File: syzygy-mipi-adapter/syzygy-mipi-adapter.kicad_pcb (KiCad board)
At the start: 4 copper layers, 45 x 70 mm, 79 parts, among them J1 Conn_02x06_Odd_Even, J10 501951-2230, J2 SYZYGY_STD, J3 Conn_01x02, J5 SM03B-SRSS-TB, J8 501951-2230, J9 501951-2230, Q1 DMG1024UV-7, Q2 DMG1024UV-7, U1 RP2350_80QFN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

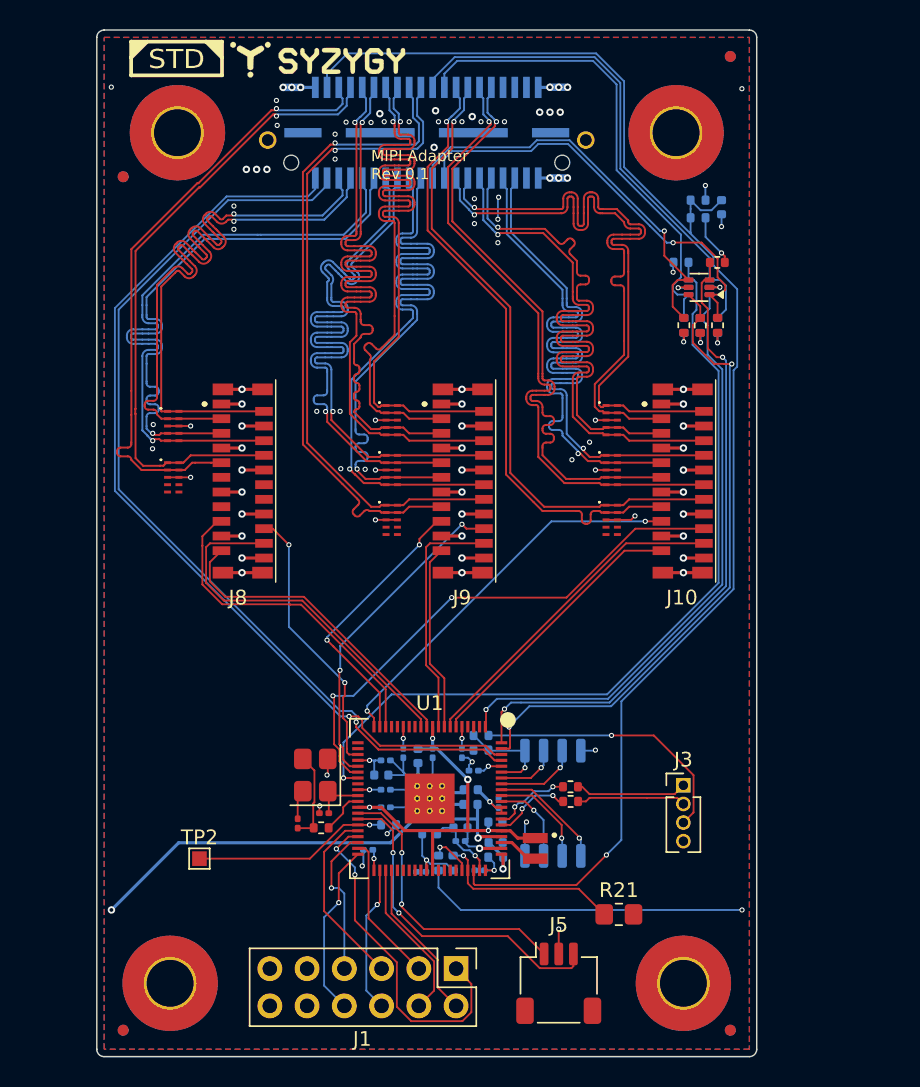
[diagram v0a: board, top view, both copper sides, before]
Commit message: Add USB connector and 3.3V regulator to Syzygy MIPI adapter
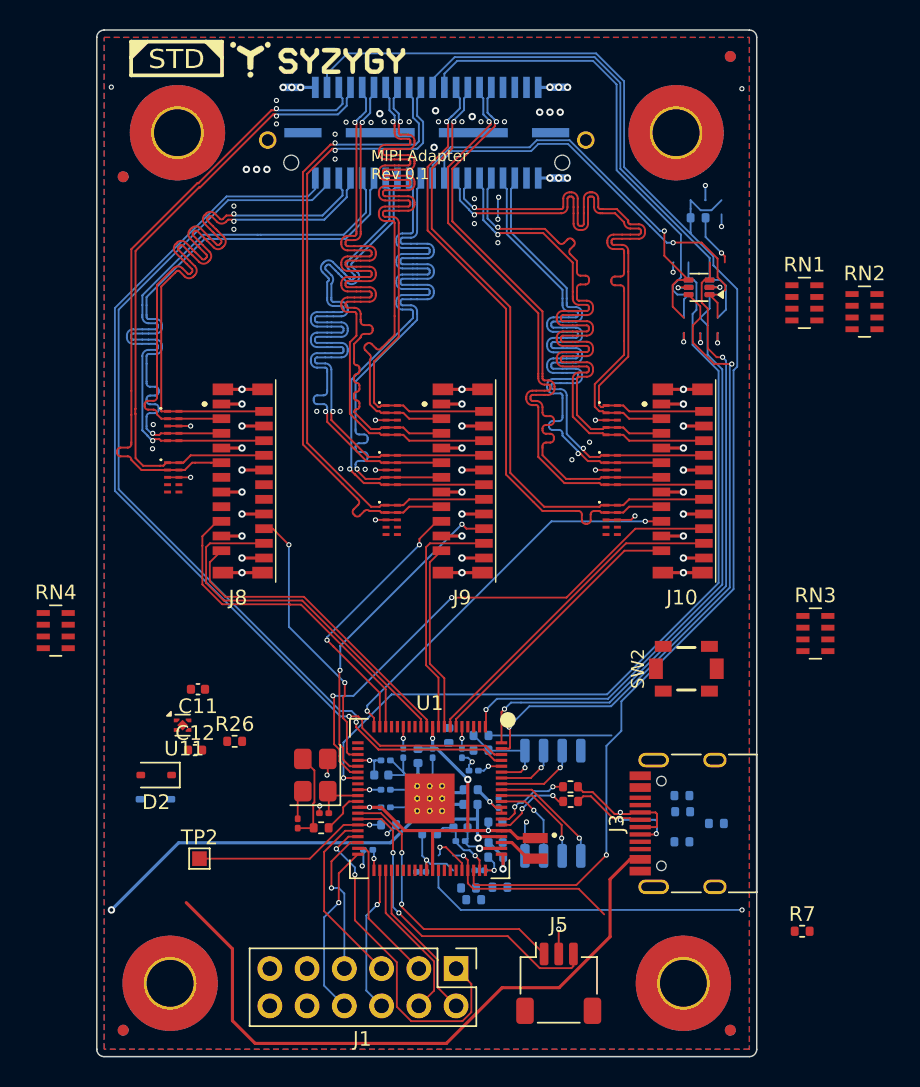
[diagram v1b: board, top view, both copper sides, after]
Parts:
- removed C44: 0.1uF, Capacitor_SMD:C_0402_1005Metric
- removed R13, R14, R15, R16, R17: 4.7K, Resistor_SMD:R_0402_1005Metric
- removed R19: ~, Resistor_SMD:R_0402_1005Metric
- removed R20: 10K, Resistor_SMD:R_0402_1005Metric
- removed R21: 0805, Resistor_SMD:R_0805_2012Metric_Pad1.20x1.40mm_HandSolder
- added C11: 10u, Capacitor_SMD:C_0402_1005Metric, F.Cu at (106.9, 105.0)
- added C12: 10u, Capacitor_SMD:C_0402_1005Metric, F.Cu at (106.7, 109.1)
- added D1: 1N5819WS, Diode_SMD:D_SOD-323, B.Cu at (104.0, 112.5)
- added D2: 1N5819WS, Diode_SMD:D_SOD-323, F.Cu at (104.0, 110.8)
- added LOGO3: OSHW logo, CUSTOM:OSHW_Dual_0.1_Scale_2140, F.Cu at (159.2, 97.0)
- added LOGO4: tinyAI logo, CUSTOM:tinyAI_logo, F.Cu at (159.9, 93.8)
- added R22: 5.1K, Resistor_SMD:R_0402_1005Metric, B.Cu at (139.9, 115.3)
- added R23: 56K, Resistor_SMD:R_0402_1005Metric, B.Cu at (139.9, 112.2)
- added R24: 56K, Resistor_SMD:R_0402_1005Metric, B.Cu at (142.2, 114.1)
- added R25: 5.1K, Resistor_SMD:R_0402_1005Metric, B.Cu at (139.9, 113.3)
- added R26: 10K, Resistor_SMD:R_0402_1005Metric, F.Cu at (109.4, 108.5)
- added R27: 15K, Resistor_SMD:R_0402_1005Metric, B.Cu at (124.0, 108.1)
- added RN1: 4.7K, Resistor_SMD:R_Array_Concave_4x0603, F.Cu at (148.2, 78.6)
- added RN2: 4.7K, Resistor_SMD:R_Array_Concave_4x0603, F.Cu at (152.3, 79.2)
- added RN3: 4.7K, Resistor_SMD:R_Array_Concave_4x0603, F.Cu at (149.0, 101.2)
- added RN4: 4.7K, Resistor_SMD:R_Array_Concave_4x0603, F.Cu at (97.2, 101.0)
- added SW2: CS1213AGF260, CUSTOM:PTS820J25KSMTRLFS, F.Cu at (140.2, 103.5)
- added U11: NCP115AMX330TCG, Package_DFN_QFN:OnSemi_XDFN4-1EP_1.0x1.0mm_EP0.52x0.52mm, F.Cu at (105.8, 107.4)
- J3: value Conn_01x02 -> USB_C_Receptacle_USB2.0_16P; footprint Connector_PinHeader_1.27mm:PinHeader_1x04_P1.27mm_Vertical -> Connector_USB:USB_C_Receptacle_HRO_TYPE-C-31-M-12
- R10: value 4.7K -> 10K; moved to B.Cu
- R11: value 4.7K -> 56K; moved to B.Cu
- R12: value 4.7K -> 56K
- R7: value 100 -> 10K; moved to F.Cu
- moved R10 45.1 mm to (127.5, 118.5)
- moved R12 45.1 mm to (125.3, 118.5)
- moved R11 42.1 mm to (125.7, 119.3), turned to 0 degrees
- moved R7 25.2 mm to (148.1, 121.5), turned to 0 degrees
- moved J3 2.82 mm to (141.1, 114.1), turned to 90 degrees
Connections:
- C1 pad 1: P5VD -> Net-(D1-K)
- J2 pad 40: P3V3D -> /SZG_3V3
- R10 pad 1: P3V3D -> /SZG_3V3
- R10 pad 2: /SCL_HOST_3V3 -> Net-(U1-GPIO44_ADC4)
- R11 pad 1: P3V3D -> Net-(U1-GPIO44_ADC4)
- R11 pad 2: /SDA_HOST_3V3 -> GND
- R12 pad 1: P3V3D -> Net-(U1-GPIO45_ADC5)
- R12 pad 2: /GPIO_HOST_3V3 -> GND
- R18 pad 1: P3V3D -> /R_GA
- R18 pad 2: /R_GA -> /SZG_3V3
- R5 pad 1: Net-(J3-Pin_1) -> /USB_D+
- R6 pad 1: Net-(J3-Pin_2) -> /USB_D-
- R8 pad 1: /USB_BOOTn -> Net-(R8-Pad1)
- U1 pad 55: unconnected-(U1-GPIO44_ADC4-Pad55) -> Net-(U1-GPIO44_ADC4)
- U1 pad 64: P5VD -> Net-(D1-K)
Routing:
- net PVBUS: track 0.00 -> 45.3 mm
- net P5VD: track 46.7 -> 15.1 mm, vias 6 -> 4
- net Net-(D1-K): track 0.00 -> 31.5 mm, vias 0 -> 2
- net /USB_BOOTn: track 18.6 -> 0.00 mm, vias 1 -> 0
- net /USB_D-: track 0.00 -> 9.71 mm, vias 0 -> 2
- net Net-(R8-Pad1): track 0.00 -> 8.39 mm
- net /USB_D+: track 0.00 -> 8.35 mm, vias 0 -> 1
- net Net-(J3-Pin_1): track 7.65 -> 0.00 mm
- net Net-(J3-Pin_2): track 7.59 -> 0.00 mm
- net P3V3D: track 37.5 -> 32.1 mm, vias 20 -> 16
- net /R_GA: track 98.5 -> 102.1 mm, vias 1 -> 2
- net /SZG_3V3: track 0.00 -> 1.80 mm, vias 0 -> 3
- net GND: track 94.4 -> 93.4 mm, vias 81 -> 80

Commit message: Add USB connector and 3.3V regulator
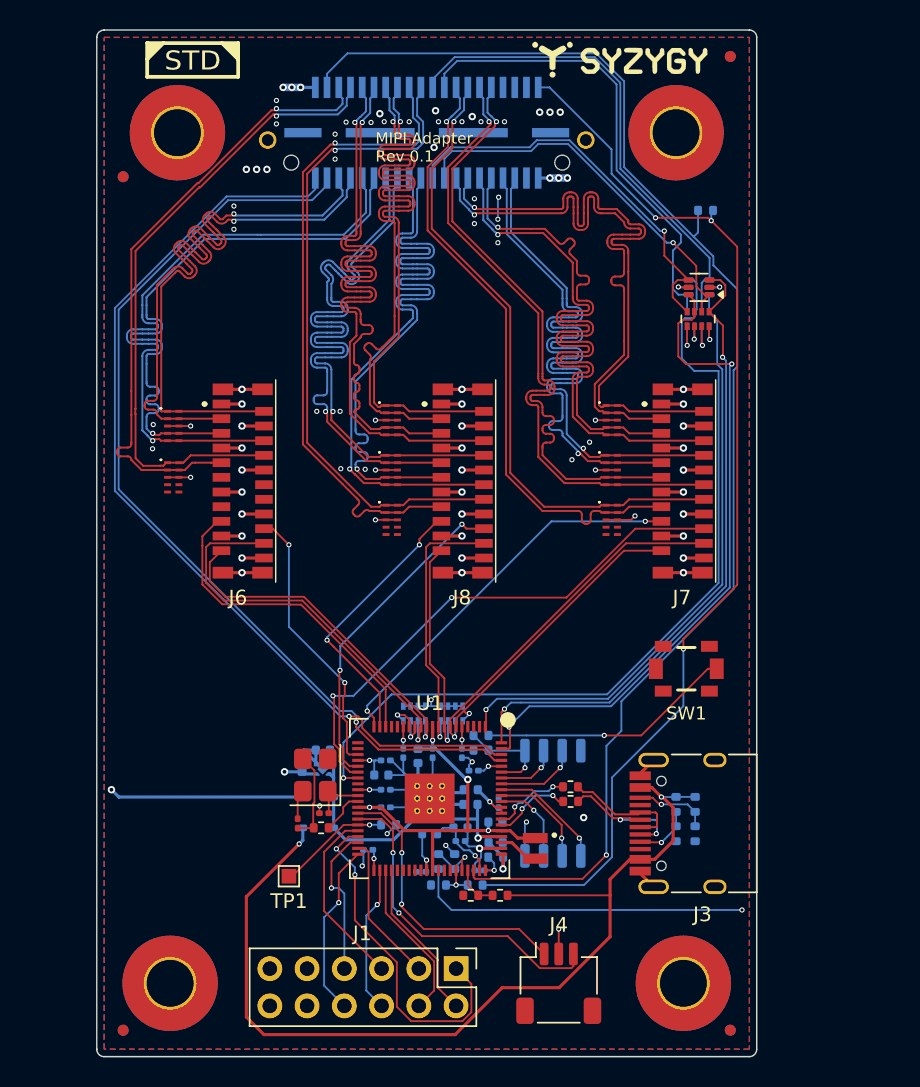
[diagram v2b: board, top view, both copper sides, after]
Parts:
- C11, C12, D2, R7, U11: moved to B.Cu
- R27: moved to F.Cu
- RN1: footprint Resistor_SMD:R_Array_Concave_4x0603 -> Resistor_SMD:R_Array_Concave_4x0402
- RN2, RN3, RN4: footprint Resistor_SMD:R_Array_Concave_4x0603 -> Resistor_SMD:R_Array_Concave_4x0402; moved to B.Cu
- SW1: renamed from SW2; value CS1213AGF260 -> ~
- moved LOGO4 48.5 mm to (122.5, 62.9)
- moved LOGO3 39.4 mm to (131.5, 125.0)
- moved RN3 25.4 mm to (124.2, 106.6), turned to 90 degrees
- moved R7 25.3 mm to (123.3, 116.7), turned to 90 degrees
- moved RN4 25.1 mm to (121.7, 106.6), turned to 90 degrees
- moved R26 20.9 mm to (127.5, 119.0), turned to 180 degrees
- moved LOGO2 20.6 mm to (135.6, 62.0)
- moved RN2 11.4 mm to (141.0, 79.7), turned to -90 degrees
- moved D1 11.3 mm to (115.1, 114.4)
- moved D2 11.2 mm to (115.1, 112.3)
- moved R27 11.0 mm to (125.5, 119.0), turned to 180 degrees
- moved U11 10.0 mm to (115.4, 110.4)
- moved C11 9.48 mm to (115.4, 109.1)
- moved C12 7.37 mm to (114.0, 110.1), turned to 90 degrees
- moved RN1 7.33 mm to (141.0, 79.7), turned to -90 degrees
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- renumbered J5 to J4, J8 to J6, J10 to J7, J9 to J8, TP2 to TP1
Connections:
- RN1 pad 1: /SCL_HOST -> /SCL_HOST_3V3
- RN1 pad 2: /SCL_HOST_3V3 -> /SDA_HOST
- RN1 pad 3: /SDA_HOST -> /SDA_HOST_3V3
- RN1 pad 4: /SDA_HOST_3V3 -> /SCL_HOST
- RN1 pad 5: P3V3D -> PVIOD
- RN1 pad 6: PVIOD -> P3V3D
- RN1 pad 7: P3V3D -> PVIOD
- RN1 pad 8: PVIOD -> P3V3D
- RN2 pad 1: /GPIO_HOST -> /BYPASSn
- RN2 pad 3: /BYPASSn -> /GPIO_HOST
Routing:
- net /SZG_3V3: track 1.80 -> 74.6 mm
- net PVBUS: track 45.3 -> 66.2 mm, vias 0 -> 2
- net P5VD: track 15.1 -> 28.4 mm
- net Net-(D1-K): track 31.5 -> 20.5 mm, vias 2 -> 1
- net Net-(U1-GPIO46_ADC6): track 12.9 -> 3.20 mm, vias 1 -> 0
- net Net-(R8-Pad1): track 8.39 -> 17.4 mm, vias 0 -> 1
- net /R_GA: track 102.1 -> 94.9 mm, vias 2 -> 1
- net GND: track 93.4 -> 100.5 mm, vias 80 -> 79
- net P3V3D: track 32.1 -> 38.1 mm, vias 16 -> 18
- net /RESETn: track 13.3 -> 7.74 mm
- net Net-(J3-CC2): track 0.00 -> 5.12 mm, vias 0 -> 1
- net Net-(J3-CC1): track 0.00 -> 3.95 mm, vias 0 -> 1
- net /SDA_HOST: track 29.0 -> 26.3 mm
- net Net-(U1-GPIO44_ADC4): track 0.00 -> 2.48 mm, vias 0 -> 1
- net /SDA1: track 12.7 -> 15.1 mm, vias 0 -> 1
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
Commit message: Add I2C test pads
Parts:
- added TP2: TestPoint, TestPoint:TestPoint_Pad_1.0x1.0mm, F.Cu at (110.0, 100.0)
- added TP3: TestPoint, TestPoint:TestPoint_Pad_1.0x1.0mm, F.Cu at (110.0, 102.0)
- added TP4: TestPoint, TestPoint:TestPoint_Pad_1.0x1.0mm, F.Cu at (124.9, 100.0)
- added TP5: TestPoint, TestPoint:TestPoint_Pad_1.0x1.0mm, F.Cu at (124.9, 102.0)
- added TP6: TestPoint, TestPoint:TestPoint_Pad_1.0x1.0mm, F.Cu at (134.5, 100.0)
- added TP7: TestPoint, TestPoint:TestPoint_Pad_1.0x1.0mm, F.Cu at (134.5, 102.0)
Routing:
- net /SDA2: track 20.4 -> 24.8 mm
- net /SCL2: track 24.7 -> 27.9 mm
- net /SDA1: track 15.1 -> 17.0 mm
- net /GPIO00: track 23.0 -> 24.9 mm
- net /SCL1: track 18.8 -> 20.1 mm
- net /SCL0: track 27.8 -> 28.9 mm
- net /SDA0: track 23.4 -> 24.1 mm
- net /GPIO10: track 18.9 -> 19.5 mm
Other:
- board text added: "SCL"
- board text added: "SDA"

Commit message: Cut out power planes under differential pair pads
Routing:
- net GND: track 100.5 -> 130.5 mm, vias 79 -> 78

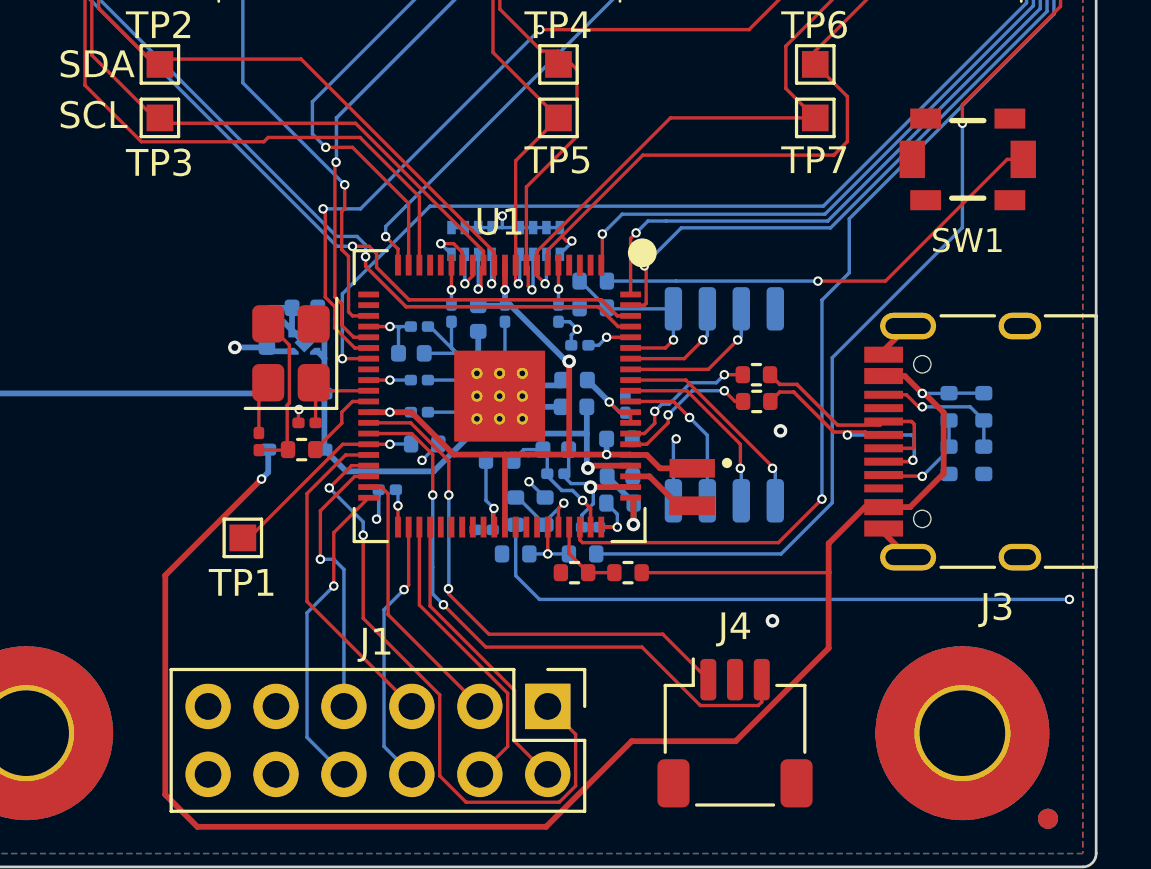
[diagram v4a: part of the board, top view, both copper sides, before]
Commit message: Oscillator ground shielding. Improve USB routing.
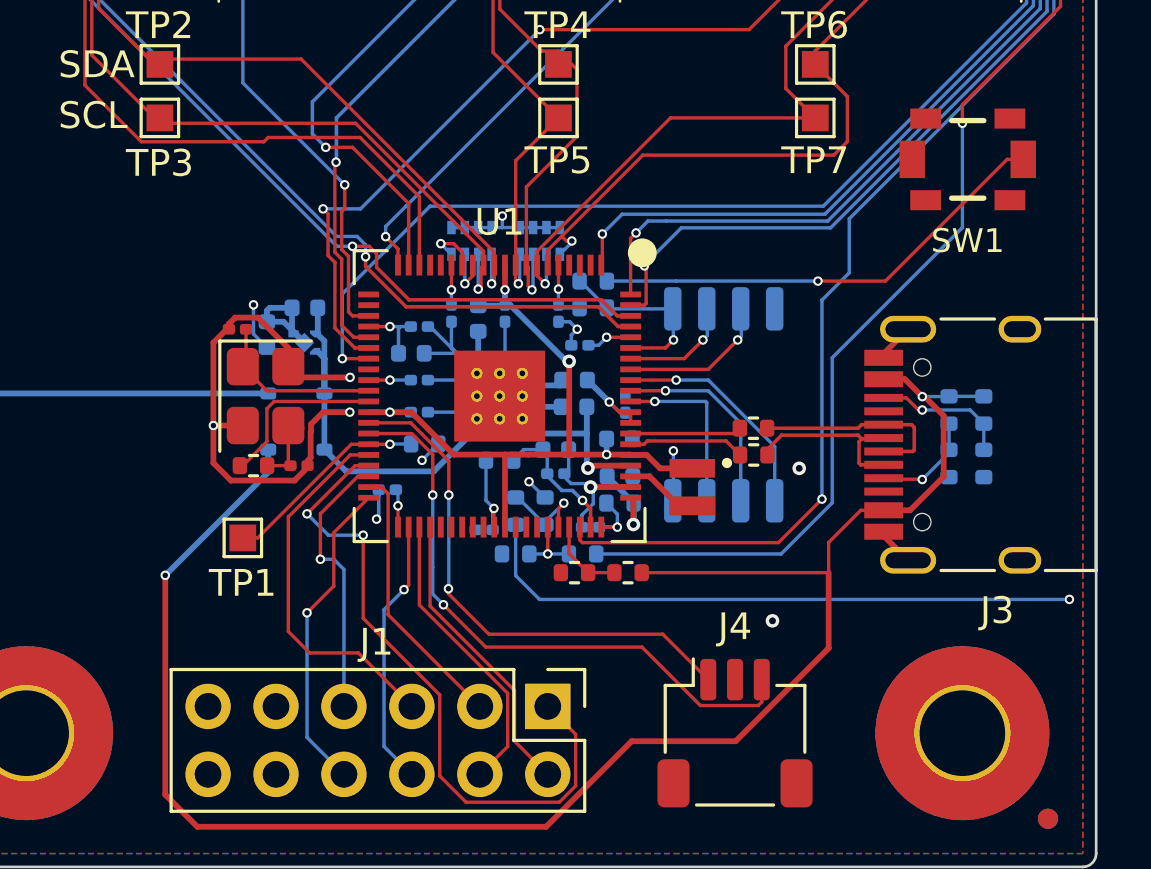
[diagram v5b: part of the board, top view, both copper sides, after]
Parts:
- moved C3 4.36 mm to (112.9, 109.9)
- moved R5 2.00 mm to (132.2, 113.6)
- moved R6 2.00 mm to (132.2, 114.6)
- moved R3 1.90 mm to (113.5, 115.0), turned to 0 degrees
- moved Y1 1.86 mm to (114.0, 112.4), turned to -90 degrees
- moved C4 1.75 mm to (115.2, 115.0), turned to 0 degrees
- moved J3 0.12 mm to (141.1, 114.2)
- moved R22 0.12 mm to (139.5, 114.9)
- moved R23 0.12 mm to (139.5, 112.9)
- moved R24 0.12 mm to (140.8, 112.9)
- moved R25 0.12 mm to (140.8, 114.9)
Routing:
- net GND: track 130.5 -> 148.2 mm, vias 78 -> 80
- net /XOUT: track 2.98 -> 6.53 mm
- net Net-(C4-Pad1): track 6.17 -> 2.73 mm
- net /XIN: track 3.71 -> 6.53 mm
- net /USB_D-: track 9.71 -> 7.31 mm, vias 2 -> 0
- net Net-(J1-Pin_5): track 12.5 -> 14.0 mm
- net Net-(J1-Pin_1): track 23.4 -> 24.8 mm
- net Net-(D1-K): track 20.5 -> 21.8 mm
- net Net-(U1-USB_DP): track 5.37 -> 4.17 mm, vias 2 -> 0
- net Net-(U1-USB_DM): track 5.46 -> 4.36 mm, vias 2 -> 0
- net /RP_QSPI.SD3: track 5.84 -> 6.53 mm
- net /USB_D+: track 8.28 -> 7.61 mm
